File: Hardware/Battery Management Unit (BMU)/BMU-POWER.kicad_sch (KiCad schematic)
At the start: 18 parts, among them Q1 DMP3099L, SW1 Power Switch, U1 OKI-78SR-5_1.5-W36-C, U2 TLV75533PDBV

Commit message: Both boards are now fully completed: the BMU and CMU.
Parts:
- TP12, TP13, TP14, TP15, TP16: symbol Connector:TestPoint_Small -> Connector:TestPoint_Square
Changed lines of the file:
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@@
 	)
 	(symbol
-		(lib_id "Connector:TestPoint_Small")
+		(lib_id "Connector:TestPoint_Square")
 		(at 187.96 140.97 0)
 		(unit 1)
@@
 		(fields_autoplaced yes)
 		(property "Reference" "TP13"
-			(at 189.23 139.6999 0)
+			(at 190.5 140.9699 0)
 			(show_name no)
 			(do_not_autoplace no)
@@
 			)
 		)
-		(property "Datasheet" ""
+		(property "Datasheet" "~"
 			(at 193.04 140.97 0)
 			(hide yes)
@@
 	)
 	(symbol
-		(lib_id "Connector:TestPoint_Small")
+		(lib_id "Connector:TestPoint_Square")
 		(at 232.41 132.08 0)
 		(unit 1)
@@
 		(fields_autoplaced yes)
 		(property "Reference" "TP15"
-			(at 233.68 130.8099 0)
+			(at 234.95 132.0799 0)
 			(show_name no)
 			(do_not_autoplace no)
@@
 			)
 		)
-		(property "Datasheet" ""
+		(property "Datasheet" "~"
 			(at 237.49 132.08 0)
 			(hide yes)
@@
 	)
 	(symbol
-		(lib_id "Connector:TestPoint_Small")
+		(lib_id "Connector:TestPoint_Square")
 		(at 128.27 133.35 0)
 		(unit 1)
@@
 		(fields_autoplaced yes)
 		(property "Reference" "TP12"
-			(at 129.54 132.0799 0)
+			(at 130.81 133.3499 0)
 			(show_name no)
 			(do_not_autoplace no)
@@
 			)
 		)
-		(property "Datasheet" ""
+		(property "Datasheet" "~"
 			(at 133.35 133.35 0)
 			(hide yes)
@@
 	)
 	(symbol
-		(lib_id "Connector:TestPoint_Small")
+		(lib_id "Connector:TestPoint_Square")
 		(at 210.82 160.02 180)
 		(unit 1)
@@
 		(fields_autoplaced yes)
 		(property "Reference" "TP14"
-			(at 209.55 161.2901 0)
-			(show_name no)
-			(do_not_autoplace no)
-			(effects
-				(font
-					(size 1.27 1.27)
-				)
-				(justify left)
+			(at 213.36 160.0199 0)
+			(show_name no)
+			(do_not_autoplace no)
+			(effects
+				(font
+					(size 1.27 1.27)
+				)
+				(justify right)
 			)
 		)
@@
 			)
 		)
-		(property "Datasheet" ""
+		(property "Datasheet" "~"
 			(at 205.74 160.02 0)
 			(hide yes)
@@
 	)
 	(symbol
-		(lib_id "Connector:TestPoint_Small")
+		(lib_id "Connector:TestPoint_Square")
 		(at 252.73 132.08 0)
 		(unit 1)
@@
 		(fields_autoplaced yes)
 		(property "Reference" "TP16"
-			(at 254 130.8099 0)
+			(at 255.27 132.0799 0)
 			(show_name no)
 			(do_not_autoplace no)
@@
 			)
 		)
-		(property "Datasheet" ""
+		(property "Datasheet" "~"
 			(at 257.81 132.08 0)
 			(hide yes)

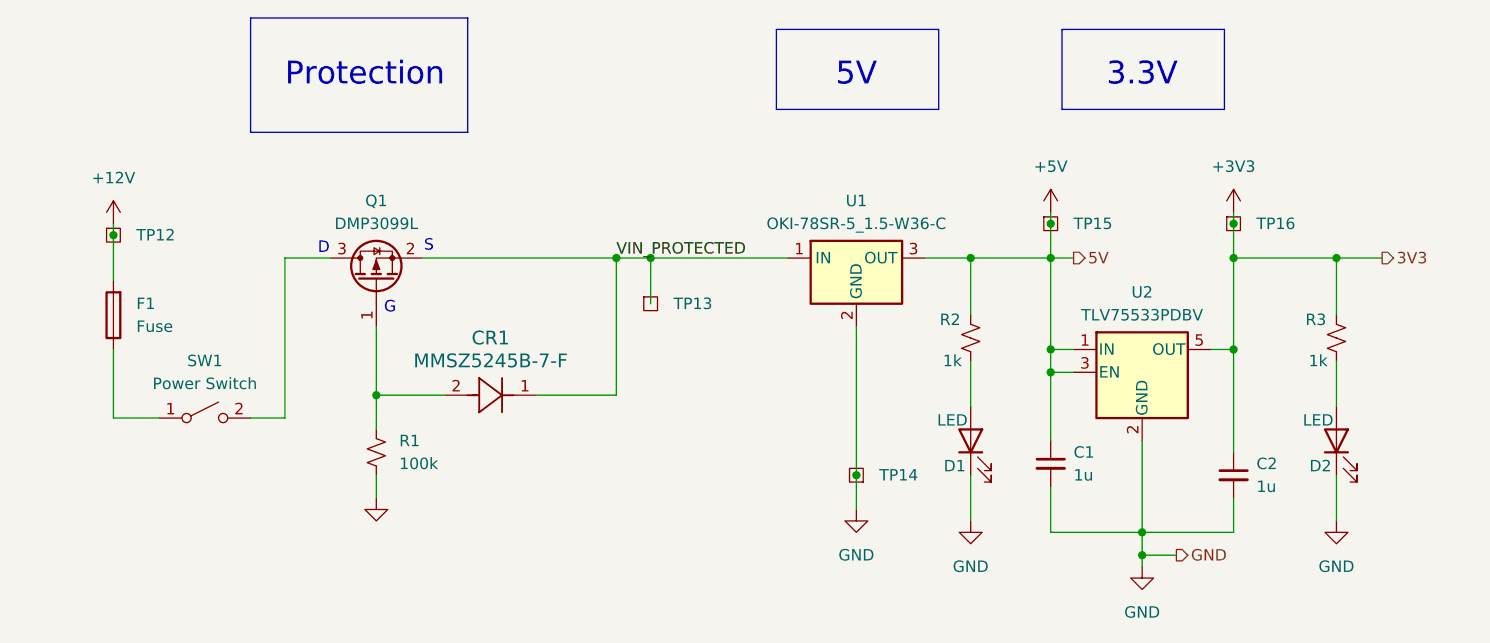
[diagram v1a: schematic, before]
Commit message: Schematic polish -- fixed to best standards, cleaned up for ERCs, etc
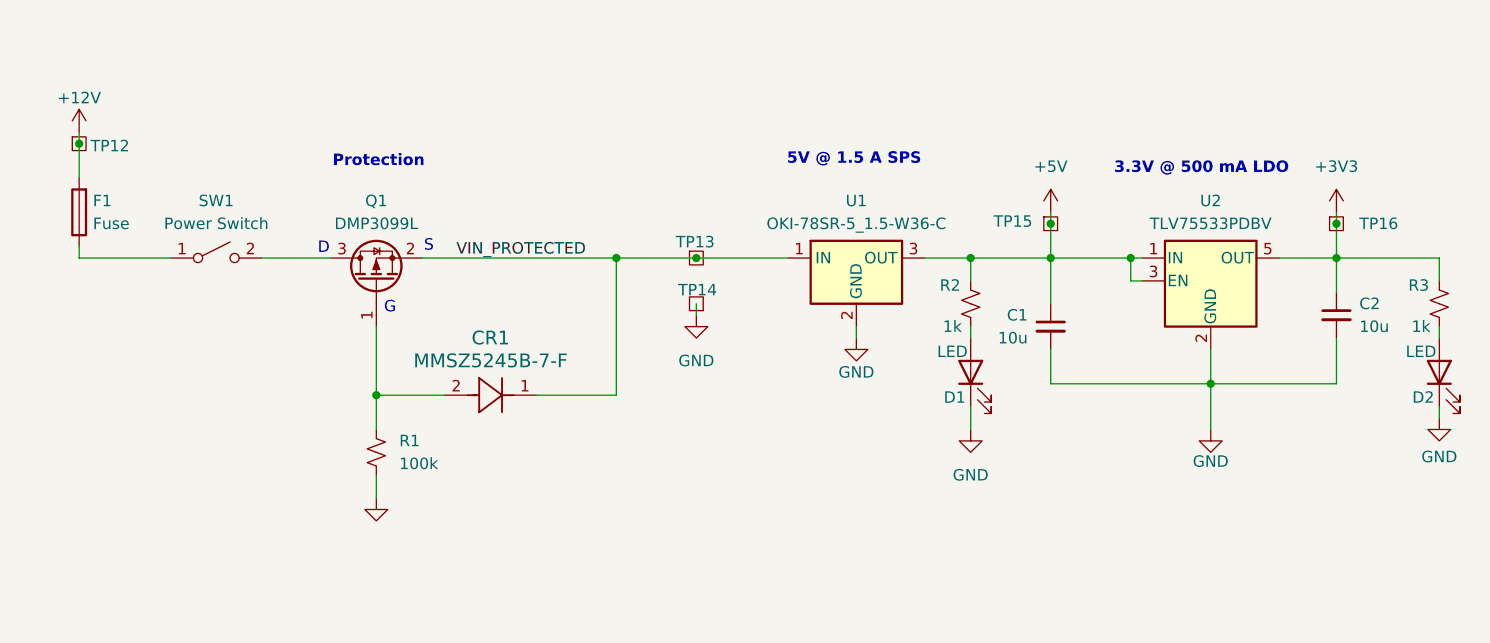
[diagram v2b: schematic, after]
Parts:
- C1, C2: value 1u -> 10u
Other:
- note added: "3.3V @ 500 mA LDO"
- note added: "5V @ 1.5 A SPS"
- note removed: "3.3V"
- note removed: "5V"
- moved on the sheet: C1, C2, D1, D2, F1, R2, R3, SW1, TP12, TP13, TP14, TP16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

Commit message: update libraries+bmu
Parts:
- CR1: footprint MMSZ5245B-7-F:SOD123_DIO -> Footprints:SOD123_DIO
- renumbered TP15 to TP10, TP16 to TP11, TP12 to TP7, TP13 to TP8, TP14 to TP9
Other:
- moved on the sheet: C1, D2, R3, TP10, TP9, U1

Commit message: Schematic cleanup; lots of missing library files
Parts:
- D1, D2: value LED -> GRN
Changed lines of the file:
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@@
 			)
 		)
-		(property "Value" "LED"
+		(property "Value" "GRN"
 			(at 274.828 146.304 90)
 			(show_name no)
@@
 			)
 		)
-		(property "Value" "LED"
+		(property "Value" "GRN"
 			(at 221.488 146.304 90)
 			(show_name no)

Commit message: Fixed all missing symbol and footprint libraries
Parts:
- CR1: symbol 2026-04-30_03-58-02:MMSZ5245B-7-F -> MMSZ5245B_7_F:MMSZ5245B-7-F
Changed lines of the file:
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@@
 	)
 	(symbol
-		(lib_id "2026-04-30_03-58-02:MMSZ5245B-7-F")
+		(lib_id "MMSZ5245B_7_F:MMSZ5245B-7-F")
 		(at 165.1 151.13 0)
 		(unit 1)

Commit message: finish! update bmu layout+BOM
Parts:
- removed Q1: DMP3099L, Package_TO_SOT_SMD:SOT-23, symbol Transistor_FET:DMP3099L
- added Q1: AO3401A, Package_TO_SOT_SMD:SOT-23, symbol Transistor_FET:AO3401A
- C1, C2: DIS (none) -> DigiKey; DPN (none) -> 311-1869-1-ND; MFR (none) -> YAGEO; MPN (none) -> CC0805KKX5R8BB106; Purchase Link (none) -> https://www.digikey.com/en/products/detail/yageo/CC0805KKX5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
- CR1: DIS (none) -> DigiKey; DPN (none) -> MMSZ5245B-FDICT-ND; MFR (none) -> Diodes Incorporated; MPN (none) -> MMSZ5245B-7-F; Purchase Link (none) -> https://www.digikey.com/en/products/detail/diodes-incorpora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
- D1, D2: DIS (none) -> DigiKey; DPN (none) -> 160-1179-1-ND; MFR (none) -> Lite-On Inc.; MPN (none) -> LTST-C170GKT; Purchase Link (none) -> https://www.digikey.com/en/products/detail/liteon/LTST-C170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
- F1: DIS (none) -> DigiKey; DPN (none) -> F1456CT-ND; MFR (none) -> Littelfuse Inc.; MPN (none) -> 0466001.NR; Purchase Link (none) -> https://www.digikey.com/en/products/detail/littelfuse-inc/0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
- R1: DIS (none) -> DigiKey; DPN (none) -> 311-100KCRCT-ND; MFR (none) -> YAGEO; MPN (none) -> RC0805FR-07100KL; Purchase Link (none) -> https://www.digikey.com/en/products/detail/yageo/RC0805FR-0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
- R2, R3: DIS (none) -> DigiKey; DPN (none) -> 311-1.00KCRCT-ND; MFR (none) -> YAGEO; MPN (none) -> RC0805FR-071KL; Purchase Link (none) -> https://www.digikey.com/en/products/detail/yageo/RC0805FR-0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
- SW1: DIS (none) -> DigiKey; DPN (none) -> 2223-DS01-254-L-01BE-ND; MFR (none) -> Same Sky; MPN (none) -> DS01-254-L-01BE; Purchase Link (none) -> https://www.digikey.com/en/products/detail/same-sky-formerl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
- U1: DIS (none) -> DigiKey; DPN (none) -> 811-2196-5-ND; MFR (none) -> Murata Power Solutions Inc.; MPN (none) -> OKI-78SR-5/1.5-W36-C; Purchase Link (none) -> https://www.digikey.com/en/products/detail/murata-power-sol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
- U2: DIS (none) -> DigiKey; DPN (none) -> 296-50411-1-ND; MFR (none) -> Texas Instruments; MPN (none) -> TLV75533PDBVR; Purchase Link (none) -> https://www.digikey.com/en/products/detail/texas-instrument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
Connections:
- net VIN_PROTECTED: now also Q1.2 (S)
- net at SW1.2 (B): now also Q1.3 (D)
- net at CR1.2, R1.1: now also Q1.1 (G)

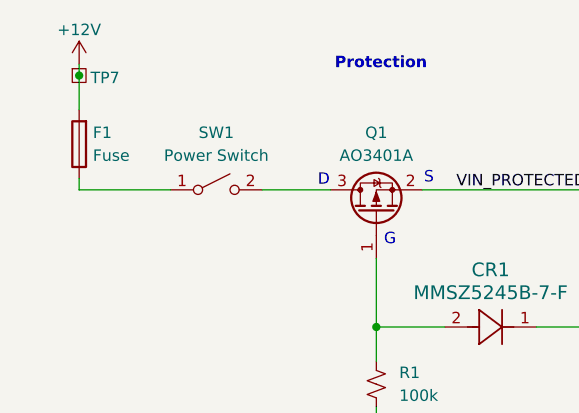
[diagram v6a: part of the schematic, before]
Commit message: add jumper+ change SW for bmu
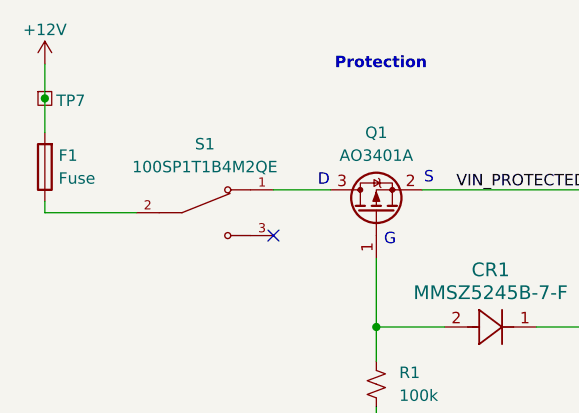
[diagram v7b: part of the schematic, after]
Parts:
- removed SW1: Power Switch, Button_Switch_THT:SW_DIP_SPSTx01_Slide_9.78x4.72mm_W7.62mm_P2.54mm, symbol Switch:SW_SPST
- added S1: 100SP1T1B4M2QE, Footprints:SW_100SP1T1B4M2QE, symbol 100SP1T1B4M2QE:100SP1T1B4M2QE
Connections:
- net at F1.1: now also S1.2
- net at Q1.3 (D): now also S1.1
- no-connect marks 0 -> 1
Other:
- moved on the sheet: F1, TP7

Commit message: Polishing, BOM fixes, stitching
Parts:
- TP10, TP11, TP7, TP8, TP9: now left out of the parts list
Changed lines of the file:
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@@
 	(title_block
 		(title "BATTERY MANAGEMENT UNIT (BMU)")
-		(date "2026-04-06")
+		(date "2026-06-02")
 		(rev "1.0")
 		(company "VIKING MOTOR SPORTS (VMS)")
@@
 		(body_style 1)
 		(exclude_from_sim no)
-		(in_bom yes)
+		(in_bom no)
 		(on_board yes)
 		(in_pos_files yes)
@@
 		(body_style 1)
 		(exclude_from_sim no)
-		(in_bom yes)
+		(in_bom no)
 		(on_board yes)
 		(in_pos_files yes)
@@
 		(body_style 1)
 		(exclude_from_sim no)
-		(in_bom yes)
+		(in_bom no)
 		(on_board yes)
 		(in_pos_files yes)
@@
 		(body_style 1)
 		(exclude_from_sim no)
-		(in_bom yes)
+		(in_bom no)
 		(on_board yes)
 		(in_pos_files yes)
@@
 		(body_style 1)
 		(exclude_from_sim no)
-		(in_bom yes)
+		(in_bom no)
 		(on_board yes)
 		(in_pos_files yes)
